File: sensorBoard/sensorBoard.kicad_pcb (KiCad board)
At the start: 4 copper layers, 203.9 x 100 mm, 164 parts, among them J10 Conn_01x07, J11 Conn_01x03, J12 Conn_01x02, J13 Conn_01x04, J14 Conn_01x05, J15 Conn_01x02, J16 Conn_01x02, J17 Conn_01x04, J18 Conn_01x07, J19 Conn_01x03, J20 Conn_01x02, J21 Conn_01x04, J22 Conn_01x05, J23 Conn_01x02, J24 Conn_01x02, J9 Conn_01x04, K5 G2RL-1-H, K6 G2RL-1-H, Q10 2N7002, Q11 2SC4213, Q12 NTD3055, Q19 2SC4213, Q2 2N7002, Q20 NTD3055, Q21 2N7002, Q22 2N7002, Q23 BSC440N10NS3G, Q24 BSC440N10NS3G, Q25 BSC440N10NS3G, Q26 BSC440N10NS3G, U12 MCP2551-I-SN, U17 LD1117S33TR_SOT223, U20 BTS50080-1TEA, U21 LM75C, U23 STM32L476RGTx, U32 BTS50080-1TEA, U33 LM75C, U35 STM32L476RGTx, U36 4011, U38 4011, U39 4011, U40 4011, U42 4N25, U43 4N25, U7 LD1117S33TR_SOT223, U9 MCP2551-I-SN, Y2 8MHz, Y3 8MHz

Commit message: finisched PCB
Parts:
- L3, L5: footprint Inductor_SMD:L_Coilcraft_XAL1580-612 -> Inductor_SMD:L_Wuerth_HCI-1890
- moved L5 0.50 mm to (163.0, 101.5)
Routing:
- net GND: vias 4038 -> 4023

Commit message: aktualisierte Platine mit verschiedenen Stecker
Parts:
- removed J11, J19: Conn_01x03, heder box:662103145021
- removed J14, J22: Conn_01x05, heder box:662105145021
- removed J15, J23: Conn_01x02, Connector_Phoenix_MC_HighVoltage:PhoenixContact_MCV_1,5_2-G-5.08_1x02_P5.08mm_Vertical
- removed J16, J24: Conn_01x02, Connector_PinHeader_2.54mm:PinHeader_1x02_P2.54mm_Vertical
- added J1: Conn_01x04, 6432101004xx:643210100404, F.Cu at (36.0, 49.0)
- added J2: Conn_01x04, 6432101004xx:643210100404, F.Cu at (36.0, 141.0)
- added J3: Conn_01x04, 6432101004xx:643210100404, F.Cu at (36.0, 118.0)
- added J4: Conn_01x04, 6432101004xx:643210100404, F.Cu at (36.0, 72.0)
- added J5: Conn_01x04, 6432101004xx:643210100404, F.Cu at (146.0, 72.0)
- added J6: Conn_01x04, 6432101004xx:643210100404, F.Cu at (146.0, 118.0)
- added J7: Conn_01x04, 6432101004xx:643210100404, F.Cu at (146.0, 141.0)
- added J8: Conn_01x04, 6432101004xx:643210100404, F.Cu at (146.0, 49.0)
- J13, J21: footprint Connector_Phoenix_MC_HighVoltage:PhoenixContact_MCV_1,5_4-G-5.08_1x04_P5.08mm_Vertical -> 6432101004xx:643210100404
- J17, J9: footprint Connector_Phoenix_MC_HighVoltage:PhoenixContact_MCV_1,5_4-G-5.08_1x04_P5.08mm_Vertical -> heder box:662104145021
- moved D5 108.4 mm to (65.2, 28.0)
- moved R5 108.4 mm to (60.8, 28.0)
- moved D3 102.7 mm to (65.1, 31.0)
- moved R3 102.7 mm to (60.7, 31.1)
- moved D2 101.1 mm to (169.4, 32.9)
- moved D4 101.1 mm to (169.4, 29.8)
- moved D6 101.1 mm to (169.4, 26.8)
- moved R2 101.1 mm to (165.0, 32.9)
- moved R4 101.1 mm to (165.0, 29.9)
- moved R6 101.1 mm to (165.0, 27.0)
- moved D1 97.2 mm to (65.1, 34.0)
- moved R1 97.2 mm to (60.7, 34.0)
- moved J18 79.2 mm to (206.0, 23.2), turned to -90 degrees
- moved J10 78.8 mm to (98.6, 24.0), turned to -90 degrees
- moved J13 77.0 mm to (36.0, 95.0), turned to -90 degrees
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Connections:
- J17 pad 1: /Platine2/Protection2/5V_IN -> /Platine2/Protection2/12V_IN
- J17 pad 4: /Platine2/Protection2/12V_IN -> /Platine2/Protection2/5V_IN
- J18 pad 1: /Platine2/microcontroller2/UART_RX -> /Platine2/microcontroller2/UART_TX
- J18 pad 2: /Platine2/microcontroller2/UART_TX -> /Platine2/microcontroller2/UART_RX
- J9 pad 1: /Platine1/Protection1/5V_IN -> /Platine1/Protection1/12V_IN
- J9 pad 4: /Platine1/Protection1/12V_IN -> /Platine1/Protection1/5V_IN
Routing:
- net +5V: track 307.2 -> 407.7 mm, vias 10 -> 11
- net /Platine1/SERVO_PWM: track 59.8 -> 153.7 mm, vias 2 -> 1
- net /Platine1/I2C_SDA: track 42.1 -> 133.7 mm, vias 3 -> 2
- net /Platine1/I2C_SCL: track 42.6 -> 129.7 mm, vias 3 -> 2
- net /Platine2/SERVO_PWM: track 67.7 -> 135.6 mm, vias 2 -> 3
- net +3.3V: track 330.3 -> 394.1 mm, vias 13 -> 9
- net /Platine2/I2C_SDA: track 71.3 -> 126.7 mm, vias 2 -> 3
- net /Platine2/I2C_SCL: track 77.1 -> 124.5 mm, vias 2 -> 3
- net /Platine1/Commutation1-1/SERVO_EN: track 83.7 -> 130.2 mm, vias 4 -> 2
- net Net-(Q11-C): track 46.4 -> 90.0 mm
- net /Platine2/Commutation2-2/SERVO_EN: track 96.8 -> 131.3 mm
- net +12V: track 101.7 -> 130.1 mm, vias 5 -> 0
- net GND: track 140.5 -> 116.1 mm, vias 4023 -> 5395
- net /Platine1/Commutation1-1/OVER_CURR_SERVO: track 109.8 -> 133.5 mm
- net /Platine1/LED_EN: track 58.9 -> 35.6 mm
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- added copper zone on In2.Cu, net GND
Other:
- board size 203.9 x 100 mm -> 210 x 150 mm
- board text added: "3.3v"
- board text added: "3v"
- board text added: "5v"
- board text added: "fan"
- board text added: "gnd"
- board text added: "h"
- board text added: "l"
- board text added: "lamp"
- board text added: "light sensor"
- board text added: "motor"
- board text added: "rst"
- board text added: "rx"
- board text added: "servo"
- board text added: "swclk"
- board text added: "swdio"
- board text added: "tx"
- board text removed: "+"
- board text removed: "-"
- board text removed: "12V"
- board text removed: "3.3"
- board text removed: "3.3V"
- board text removed: "5V"
- board text removed: "GND"
- board text removed: "H"
- board text removed: "L"
- board text removed: "LED_OUT"
- board text removed: "RST"
- board text removed: "RX"
- board text removed: "SCL"
- board text removed: "SDA"
- board text removed: "SWCLK"
- board text removed: "SWDIO"
- board text removed: "TX"

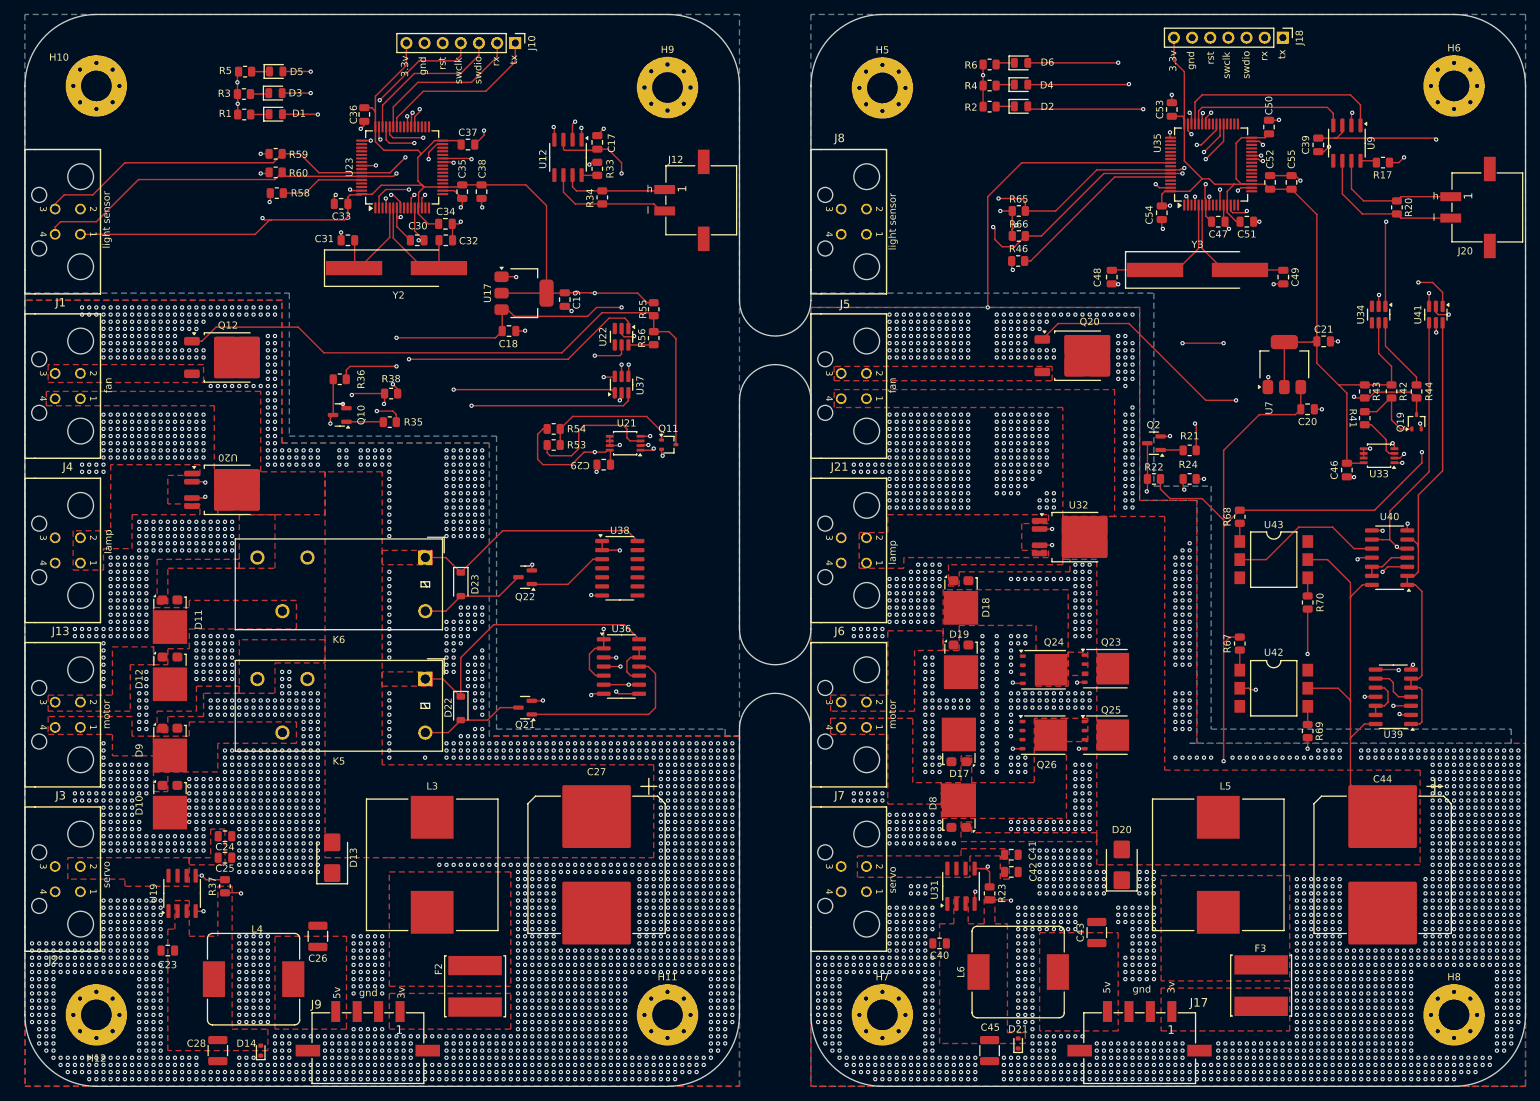
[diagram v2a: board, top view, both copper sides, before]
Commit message: added old software + new PCB
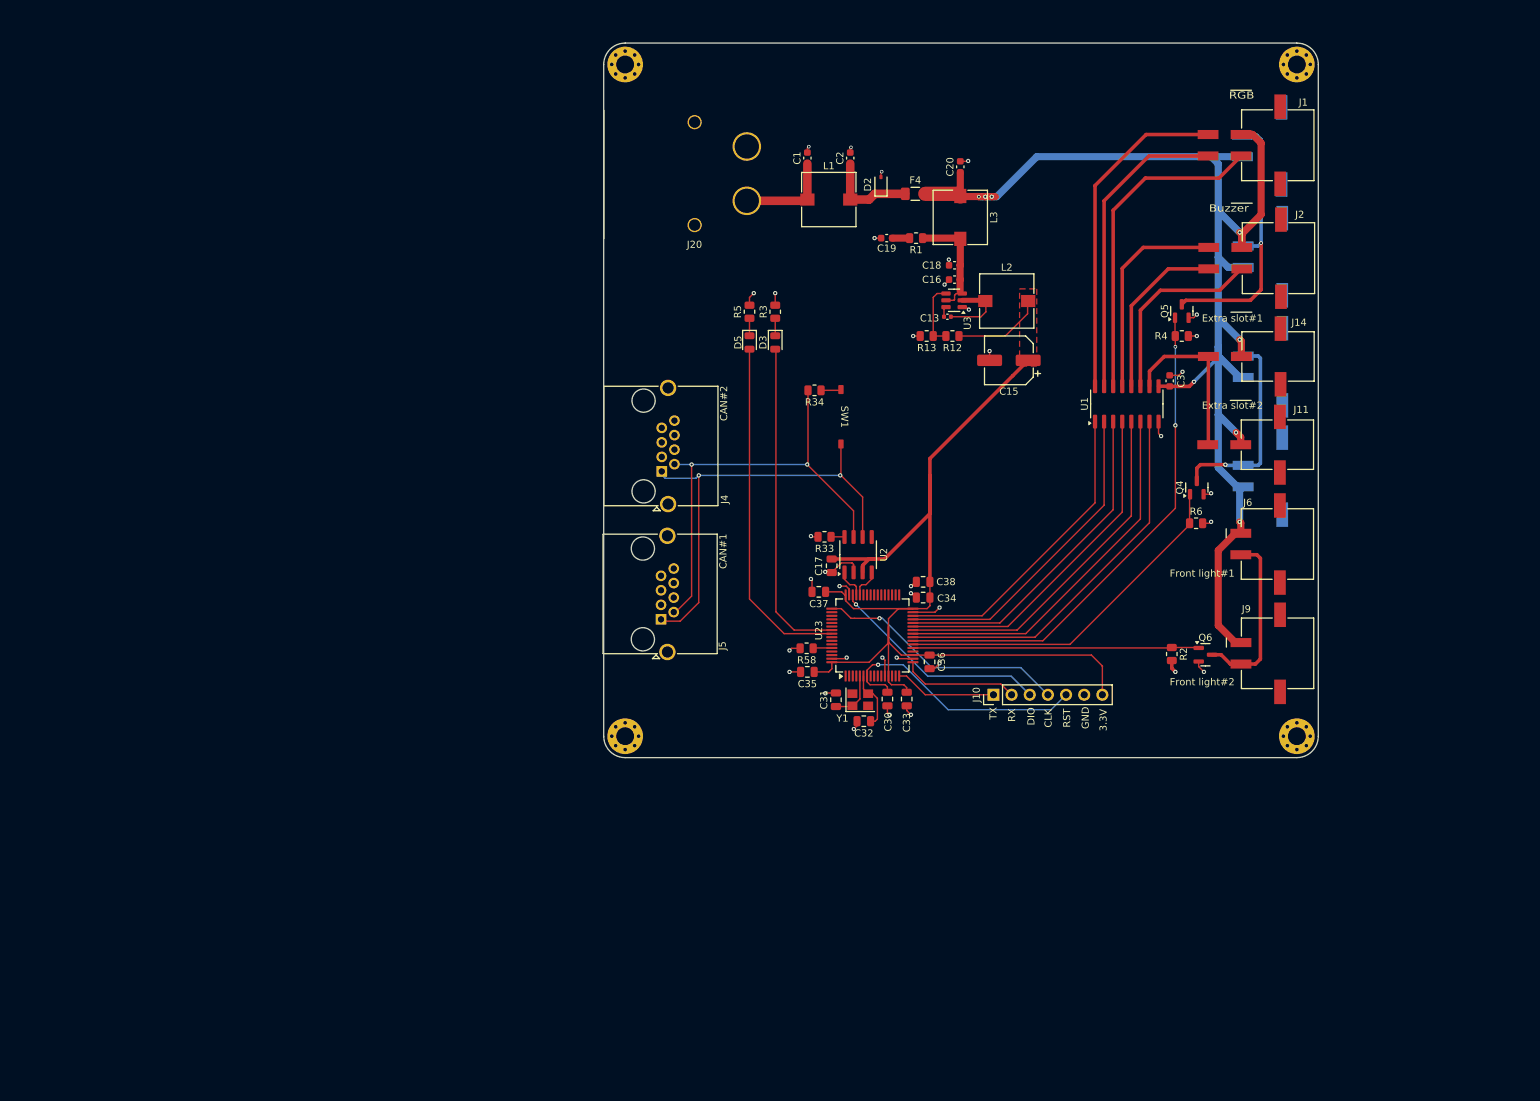
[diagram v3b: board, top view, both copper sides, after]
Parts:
- removed C21: 10µF, Capacitor_SMD:C_0805_2012Metric
- removed C23, C24, C29, C39, C40, C41, C46, C47, C50, C51, C52, C53, C54: 0.1µF, Capacitor_SMD:C_0805_2012Metric
- removed C25, C42: 22µF, Capacitor_SMD:C_0805_2012Metric
- removed C26, C28, C43, C45: 10µF, Capacitor_SMD:C_1210_3225Metric
- removed C27, C44: 2200µF, Capacitor_SMD:CP_Elec_18x17.5
- removed C48, C49: 20pF, Capacitor_SMD:C_0805_2012Metric
- removed C55: 4.7µF, Capacitor_SMD:C_0805_2012Metric
- removed D1, D4, D6: LED_Small, LED_SMD:LED_0805_2012Metric
- removed D10, D11, D12, D17, D18, D19, D8, D9: D_KAA, Package_TO_SOT_SMD:TO-277A
- removed D13, D20: ESD9B3.3ST5G, Diode_SMD:D_SMB
- removed D14, D21: ESD9B3.3ST5G, Diode_SMD:D_SOD-523
- removed D22, D23: D_Small, Diode_SMD:D_SOD-123
- removed F2, F3: Fuse_Small, Inductor_SMD:L_Cenker_CKCS8080
- removed G*** (x2): LOGO, Kicad:paltech25_25
- removed H10, H11, H12, H5, H6, H7, H8, H9: MountingHole_Pad, MountingHole:MountingHole_4.3mm_M4_Pad_Via
- removed J17: Conn_01x04, heder box:662104145021
- removed J18: Conn_01x07, Connector_PinHeader_2.54mm:PinHeader_1x07_P2.54mm_Vertical
- removed J21, J3: Conn_01x04, 6432101004xx:643210100404
- removed K5, K6: G2RL-1-H, Relay_THT:Relay_SPDT_Omron_G2RL-1
- removed L4, L6: 10µH, Inductor_SMD:L_Bourns_SRP1245A
- removed L5: 10µH, Inductor_SMD:L_Wuerth_HCI-1890
- removed Q10, Q2, Q21, Q22: 2N7002, Package_TO_SOT_SMD:SOT-23
- removed Q11, Q19: 2SC4213, Package_TO_SOT_SMD:SOT-323_SC-70
- removed Q12, Q20: NTD3055, Package_TO_SOT_SMD:TO-252-2
- removed Q23, Q24, Q25, Q26: BSC440N10NS3G, Package_TO_SOT_SMD:TDSON-8-1
- removed R17: R_Small, Resistor_SMD:R_0805_2012Metric
- removed R20: 120, Resistor_SMD:R_0805_2012Metric
- removed R21, R22, R35, R36, R69, R70: 100, Resistor_SMD:R_0805_2012Metric
- removed R23, R37, R42, R43, R46, R54, R55, R59, R60, R65, R66: 10k, Resistor_SMD:R_0805_2012Metric
- removed R24, R38: 1k, Resistor_SMD:R_0805_2012Metric
- removed R41, R44, R53, R56: 0, Resistor_SMD:R_0805_2012Metric
- removed R67, R68: 380, Resistor_SMD:R_0805_2012Metric
- removed U12, U9: MCP2551-I-SN, Package_SO:SOIC-8_3.9x4.9mm_P1.27mm
- removed U17, U7: LD1117S33TR_SOT223, Package_TO_SOT_SMD:SOT-223-3_TabPin2
- removed U19, U31: ~, Package_SO:SOIC-8_3.9x4.9mm_P1.27mm
- removed U20, U32: BTS50080-1TEA, Package_TO_SOT_SMD:TO-252-4
- removed U21, U33: LM75C, Package_SO:TSSOP-8_3x3mm_P0.65mm
- removed U22, U34, U37, U41: ~, Package_TO_SOT_SMD:SC-74-6_1.55x2.9mm_P0.95mm
- removed U35: STM32L476RGTx, Package_QFP:LQFP-64_10x10mm_P0.5mm
- removed U36, U38, U39, U40: 4011, Package_SO:SOIC-14_3.9x8.7mm_P1.27mm
- removed U42, U43: 4N25, Package_DIP:SMDIP-6_W9.53mm_Clearance8mm
- removed Y2, Y3: 8MHz, Crystal:Crystal_SMD_HC49-SD_HandSoldering
- added C1: 1µF, Capacitor_SMD:C_0603_1608Metric, F.Cu at (139.5, 40.1)
- added C13: 0.1µF, Capacitor_SMD:C_0402_1005Metric, F.Cu at (159.1, 62.3)
- added C15: 22µF, Capacitor_SMD:CP_Elec_6.3x5.8, F.Cu at (167.7, 68.4)
- added C16: 0.1µF, Capacitor_SMD:C_0603_1608Metric, F.Cu at (160.1, 57.1)
- added C2: 1µF, Capacitor_SMD:C_0603_1608Metric, F.Cu at (145.5, 40.1)
- added C3: 0.1µF, Capacitor_SMD:C_0603_1608Metric, F.Cu at (190.2, 71.3)
- added F4: Fuse_Small, Fuse:Fuse_1206_3216Metric, F.Cu at (154.6, 45.1)
- added H1: MountingHole_Pad_MP, MountingHole:MountingHole_2.5mm_Pad_Via, F.Cu at (114.0, 27.0)
- added H2: MountingHole_Pad_MP, MountingHole:MountingHole_2.5mm_Pad_Via, F.Cu at (208.0, 27.0)
- added H3: MountingHole_Pad_MP, MountingHole:MountingHole_2.5mm_Pad_Via, F.Cu at (114.0, 121.0)
- added H4: MountingHole_Pad_MP, MountingHole:MountingHole_2.5mm_Pad_Via, F.Cu at (208.0, 121.0)
- added J11: Conn_01x02, Pavel_library:J_Wurth_WR-MPC3_662002231722, F.Cu at (205.3, 80.2)
- added J14: Conn_01x02, Pavel_library:J_Wurth_WR-MPC3_662002231722, F.Cu at (205.4, 67.9)
- added L1: 1µH, Inductor_SMD:L_Wuerth_WE-PD-Typ-7345, F.Cu at (142.5, 45.9)
- added L2: 2.2µH, Inductor_SMD:L_Wuerth_WE-PD-Typ-7345, F.Cu at (167.4, 60.1)
- added Q4: Q_NMOS_Depletion_GSD, Package_TO_SOT_SMD:SOT-23, F.Cu at (194.0, 86.2)
- added Q5: Q_NMOS_Depletion_GSD, Package_TO_SOT_SMD:SOT-23, F.Cu at (191.9, 61.5)
- added Q6: Q_NMOS_Depletion_GSD, Package_TO_SOT_SMD:SOT-23, F.Cu at (195.2, 109.6)
- added R12: 100k, Resistor_SMD:R_0805_2012Metric, F.Cu at (159.8, 65.0)
- added R13: 22.1k, Resistor_SMD:R_0805_2012Metric, F.Cu at (156.2, 65.0)
- added SW1: SW_DIP_x01, Pavel_library:416131160801, F.Cu at (144.2, 76.3)
- added U1: MC1413BD, Package_SO:SOIC-16_3.9x9.9mm_P1.27mm, F.Cu at (184.2, 74.5)
- added U2: MAX3051, Package_SO:SOIC-8_3.9x4.9mm_P1.27mm, F.Cu at (146.6, 95.6)
- added U3: LMR51430, Package_TO_SOT_SMD:SOT-23-6, F.Cu at (160.0, 60.0)
- added Y1: Crystal_GND24_Small, Crystal:Crystal_SMD_3225-4Pin_3.2x2.5mm, F.Cu at (146.9, 115.9)
- C18: value 0.1µF -> 1µF; footprint Capacitor_SMD:C_0805_2012Metric -> Capacitor_SMD:C_0603_1608Metric
- C19: value 10µF -> 1µF; footprint Capacitor_SMD:C_0805_2012Metric -> Capacitor_SMD:C_0603_1608Metric
- C20: value 0.1µF -> 10µF; footprint Capacitor_SMD:C_0805_2012Metric -> Capacitor_SMD:C_0603_1608Metric
- C31, C32: value 20pF -> 18pF
- D2: value LED_Small -> TVS; footprint LED_SMD:LED_0805_2012Metric -> Diode_SMD:D_SOD-323
- J1, J2: footprint 6432101004xx:643210100404 -> Pavel_library:J_Wurth_WR-MPC3_662004231722
- J12: footprint heder box:662102145021 -> Pavel_library:J_Wurth_WR-MPC3_662102145021; moved to B.Cu
- J13, J7, J8: value Conn_01x04 -> Conn_01x02; footprint 6432101004xx:643210100404 -> Pavel_library:J_Wurth_WR-MPC3_662102145021; moved to B.Cu
- J20: value Conn_01x02 -> Conn_01x03; footprint heder box:662102145021 -> Pavel_library:Untitled
- J4, J5: value Conn_01x04 -> RJ45; footprint 6432101004xx:643210100404 -> Connector_RJ:RJ45_Amphenol_RJHSE5380
- J6: value Conn_01x04 -> Conn_01x02; footprint 6432101004xx:643210100404 -> Pavel_library:J_Wurth_WR-MPC3_662102145021
- J9: value Conn_01x04 -> Conn_01x02; footprint heder box:662104145021 -> Pavel_library:J_Wurth_WR-MPC3_662102145021
- L3: value 10µH -> 1µH; footprint Inductor_SMD:L_Wuerth_HCI-1890 -> Inductor_SMD:L_Wuerth_WE-PD-Typ-7345
- R1: value 1k -> 1.87
- R2, R4, R6: value 1k -> 10k
- R33: value R_Small -> 0
- moved J2 190.4 mm to (205.4, 54.1)
- moved J13 169.9 mm to (205.6, 84.6), turned to 0 degrees
- moved J1 169.7 mm to (205.3, 38.3)
- moved J9 138.9 mm to (205.3, 109.4)
- moved L3 116.9 mm to (160.9, 48.4), turned to -90 degrees
- moved J10 113.1 mm to (165.5, 115.2), turned to 90 degrees
- moved C36 110.1 mm to (156.6, 110.6)
- moved J7 105.5 mm to (205.6, 53.9), turned to 0 degrees
- moved C33 105.2 mm to (153.4, 115.8), turned to -90 degrees
- moved J20 104.1 mm to (131.0, 42.3), turned to -90 degrees
- moved R58 97.8 mm to (139.4, 108.7)
- moved R1 95.6 mm to (154.7, 51.3)
- moved C31 93.8 mm to (143.5, 115.9), turned to 90 degrees
- moved U23 92.8 mm to (148.6, 106.9)
- moved C30 91.9 mm to (150.7, 115.8), turned to -90 degrees
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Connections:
- C17 pad 1: +5V -> +3.3V
- C18 pad 1: +5V -> Net-(U3-EN)
- C19 pad 1: +3.3V -> Net-(C19-Pad1)
- C20 pad 1: +5V -> +24V
- D2 pad 2: Net-(D2-A) -> GND
- J1 pad 1: +3.3V -> +24V
- J1 pad 2: GND -> /Platine1/Commutation1-1/OUT3
- J1 pad 3: /Platine1/I2C_SCL -> /Platine1/Commutation1-1/OUT1
- J1 pad 4: /Platine1/I2C_SDA -> /Platine1/Commutation1-1/OUT2
- J12 pad 1: /Platine1/CAN_H -> +24V
- J12 pad 2: /Platine1/CAN_L -> /Platine1/Commutation1-1/OUT10
- J13 pad 1: /Platine1/Commutation1-1/LAMP_OUT -> +24V
- J13 pad 2: /Platine1/Commutation1-1/LAMP_OUT -> /Platine1/Commutation1-1/OUT10
- J2 pad 1: /Platine1/SERVO_PWM -> +24V
- J2 pad 2: /Platine1/Commutation1-1/SERVO_OUT -> /Platine1/Commutation1-1/OUT6
- J2 pad 3: GND -> /Platine1/Commutation1-1/OUT4
- J2 pad 4: unconnected-(J2-Pin_4-Pad4) -> /Platine1/Commutation1-1/OUT5
- J20 pad 1: /Platine2/CAN_H -> GND
- J20 pad 2: /Platine2/CAN_L -> Net-(J20-Pin_2)
- J4 pad 1: +12V -> /Platine1/CAN_L
- J4 pad 2: Net-(J4-Pin_2) -> /Platine1/CAN_H
- J4 pad 3: Net-(J4-Pin_2) -> GND
- J4 pad 4: +12V -> unconnected-(J4-Pad4)
- J5 pad 1: +12V -> /Platine1/CAN_L
- J5 pad 2: Net-(J5-Pin_2) -> /Platine1/CAN_H
- J5 pad 3: Net-(J5-Pin_2) -> GND
- J5 pad 4: +12V -> unconnected-(J5-Pad4)
- J6 pad 1: /Platine2/Commutation2-2/POLE+ -> +24V
- J6 pad 2: /Platine2/Commutation2-2/POLE- -> /Platine1/Commutation1-1/OUT8
- J7 pad 1: /Platine2/SERVO_PWM -> +24V
- J7 pad 2: /Platine2/Commutation2-2/SERVO_OUT -> /Platine1/Commutation1-1/OUT9
- J8 pad 1: +3.3V -> +24V
- J8 pad 2: GND -> /Platine1/Commutation1-1/OUT9
- J9 pad 1: /Platine1/Protection1/12V_IN -> +24V
- J9 pad 2: GND -> /Platine1/Commutation1-1/OUT8
- L3 pad 1: Net-(F2-Pad2) -> +24V
- L3 pad 2: +12V -> Net-(U3-EN)
- R1 pad 1: Net-(D1-K) -> Net-(U3-EN)
- R1 pad 2: GND -> Net-(C19-Pad1)
- R2 pad 1: Net-(D2-K) -> /Platine1/Commutation1-1/IN8
- R34 pad 1: /Platine1/CAN_H -> Net-(R34-Pad1)
- R34 pad 2: /Platine1/CAN_L -> /Platine1/CAN_H
- R4 pad 1: Net-(D4-K) -> /Platine1/Commutation1-1/IN9
- R6 pad 1: Net-(D6-K) -> /Platine1/Commutation1-1/IN10
- U23 pad 11: /Platine1/Commutation1-1/SERVO_EN -> unconnected-(U23-PC3-Pad11)
- U23 pad 14: /Platine1/SERVO_PWM -> unconnected-(U23-PA0-Pad14)
- U23 pad 16: unconnected-(U23-PA2-Pad16) -> /Platine1/microcontroller1/UART_TX
- U23 pad 17: unconnected-(U23-PA3-Pad17) -> /Platine1/microcontroller1/UART_RX
- U23 pad 2: /Platine1/TemperaturRegelung1/FAN_EN -> unconnected-(U23-PC13-Pad2)
- U23 pad 21: unconnected-(U23-PA5-Pad21) -> /Platine1/Commutation1-1/IN8
- U23 pad 22: unconnected-(U23-PA6-Pad22) -> /Platine1/Commutation1-1/IN10
- U23 pad 23: unconnected-(U23-PA7-Pad23) -> /Platine1/Commutation1-1/IN9
- U23 pad 24: unconnected-(U23-PC4-Pad24) -> /Platine1/Commutation1-1/IN7
- U23 pad 25: unconnected-(U23-PC5-Pad25) -> /Platine1/Commutation1-1/IN6
- U23 pad 26: /Platine1/DIN -> /Platine1/Commutation1-1/IN5
- U23 pad 27: /Platine1/EN_MOTOR -> /Platine1/Commutation1-1/IN4
- U23 pad 28: unconnected-(U23-PB2-Pad28) -> /Platine1/Commutation1-1/IN3
- U23 pad 29: unconnected-(U23-PB10-Pad29) -> /Platine1/Commutation1-1/IN2
- U23 pad 30: unconnected-(U23-PB11-Pad30) -> /Platine1/Commutation1-1/IN1
- U23 pad 33: unconnected-(U23-PB12-Pad33) -> /Platine1/microcontroller1/CAN_EN
- U23 pad 37: Net-(D5-A) -> unconnected-(U23-PC6-Pad37)
- U23 pad 38: Net-(D3-A) -> unconnected-(U23-PC7-Pad38)
- U23 pad 39: Net-(D1-A) -> unconnected-(U23-PC8-Pad39)
- U23 pad 4: /Platine1/LED_EN -> unconnected-(U23-PC15-Pad4)
- U23 pad 42: /Platine1/microcontroller1/UART_TX -> unconnected-(U23-PA9-Pad42)
- U23 pad 43: /Platine1/microcontroller1/UART_RX -> unconnected-(U23-PA10-Pad43)
- U23 pad 55: unconnected-(U23-PB3-Pad55) -> Net-(D3-A)
- U23 pad 56: /Platine1/Commutation1-1/OVER_CURR_SERVO -> Net-(D5-A)
- U23 pad 58: /Platine1/I2C_SCL -> unconnected-(U23-PB6-Pad58)
- U23 pad 59: /Platine1/I2C_SDA -> unconnected-(U23-PB7-Pad59)
- U23 pad 8: /Platine1/IS_DIAG -> unconnected-(U23-PC0-Pad8)
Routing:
- net +5V: track 407.7 -> 0.00 mm, vias 11 -> 0
- net +3.3V: track 394.1 -> 163.1 mm, vias 9 -> 0
- net +24V: track 0.00 -> 185.2 mm, vias 0 -> 8
- net /Platine1/SERVO_PWM: track 153.7 -> 0.00 mm, vias 1 -> 0
- net /Platine2/SERVO_PWM: track 135.6 -> 0.00 mm, vias 3 -> 0
- net /Platine1/I2C_SDA: track 133.7 -> 0.00 mm, vias 2 -> 0
- net /Platine1/Commutation1-1/OVER_CURR_SERVO: track 133.5 -> 0.00 mm, vias 2 -> 0
- net /Platine2/Commutation2-2/SERVO_EN: track 131.3 -> 0.00 mm, vias 2 -> 0
- net /Platine1/Commutation1-1/SERVO_EN: track 130.2 -> 0.00 mm, vias 2 -> 0
- net +12V: track 130.1 -> 0.00 mm
- net /Platine1/I2C_SCL: track 129.7 -> 0.00 mm, vias 2 -> 0
- net /Platine2/Commutation2-2/OVER_CURR_SERVO: track 126.8 -> 0.00 mm, vias 2 -> 0
- net /Platine2/I2C_SDA: track 126.7 -> 0.00 mm, vias 3 -> 0
- net /Platine2/I2C_SCL: track 124.5 -> 0.00 mm, vias 3 -> 0
- net Net-(Q11-C): track 90.0 -> 0.00 mm
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- added copper zone on F.Cu, net +3.3V
- removed copper zone on F.Cu, net +12V
- removed copper zone on F.Cu, net +5V
- removed copper zone on F.Cu, net /Platine1/Commutation1-1/LAMP_OUT
- removed copper zone on F.Cu, net /Platine1/Commutation1-1/POLE+
- removed copper zone on F.Cu, net /Platine1/Commutation1-1/POLE-
- removed copper zone on F.Cu, net /Platine1/Commutation1-1/SERVO_OUT
- removed copper zone on F.Cu, net /Platine1/Protection1/12V_IN
- removed copper zone on F.Cu, net /Platine1/Protection1/5V_IN
- removed copper zone on F.Cu, net /Platine2/Commutation2-2/LAMP_OUT
- removed copper zone on F.Cu, net /Platine2/Commutation2-2/POLE+
- removed copper zone on F.Cu, net /Platine2/Commutation2-2/POLE-
- removed copper zone on F.Cu, net /Platine2/Commutation2-2/SERVO_OUT
- removed copper zone on F.Cu, net /Platine2/Protection2/12V_IN
- removed copper zone on F.Cu, net /Platine2/Protection2/5V_IN
- removed copper zone on B.Cu, net GND
- removed copper zone on F.Cu, net GND
- removed copper zone on F.Cu, net Net-(F2-Pad2)
- removed copper zone on F.Cu, net Net-(F3-Pad2)
- removed copper zone on F.Cu, net Net-(J4-Pin_2)
- removed copper zone on F.Cu, net Net-(J5-Pin_2)
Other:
- board size 210 x 150 mm -> 100 x 100 mm
- board text added: "3.3V"
- board text added: "Buzzer"
- board text added: "CAN#1"
- board text added: "CAN#2"
- board text added: "CLK"
- board text added: "DIO"
- board text added: "Extra slot#1"
- board text added: "Extra slot#2"
- board text added: "Extra slot#3"
- board text added: "Extra slot#4"
- board text added: "Front light#1"
- board text added: "Front light#2"
- board text added: "GND"
- board text added: "Inner Light"
- board text added: "Inner Light#1"
- board text added: "Inner Light#2"
- board text added: "RGB"
- board text added: "RST"
- board text added: "RX"
- board text added: "TX"
- board text removed: "3.3v"
- board text removed: "3v"
- board text removed: "5v"
- board text removed: "fan"
- board text removed: "gnd"
- board text removed: "h"
- board text removed: "l"
- board text removed: "lamp"
- board text removed: "light sensor"
- board text removed: "motor"
- board text removed: "rst"
- board text removed: "rx"
- board text removed: "servo"
- board text removed: "swclk"
- board text removed: "swdio"
- board text removed: "tx"
